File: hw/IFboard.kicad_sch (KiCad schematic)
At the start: 72 parts, among them J1 USB_C_Receptacle_USB2.0_16P, J2 Conn_01x02_Socket, J3 Conn_ARM_SWD_TagConnect_TC203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, J4 Conn_01x02_Socket, J5 Conn_01x02_Socket, J6 Conn_01x02_Socket, SW3 SW_Push, SW4 SW_Push, SW5 SW_Push, SW6 SW_Push, U1 AMS1117-3.3, U2 XC6206PxxxMR, U3 TCAN3413DR, U4 ST4E1240DT, U5 MAX232ESE+T, U6 STM32G0B1CBTx

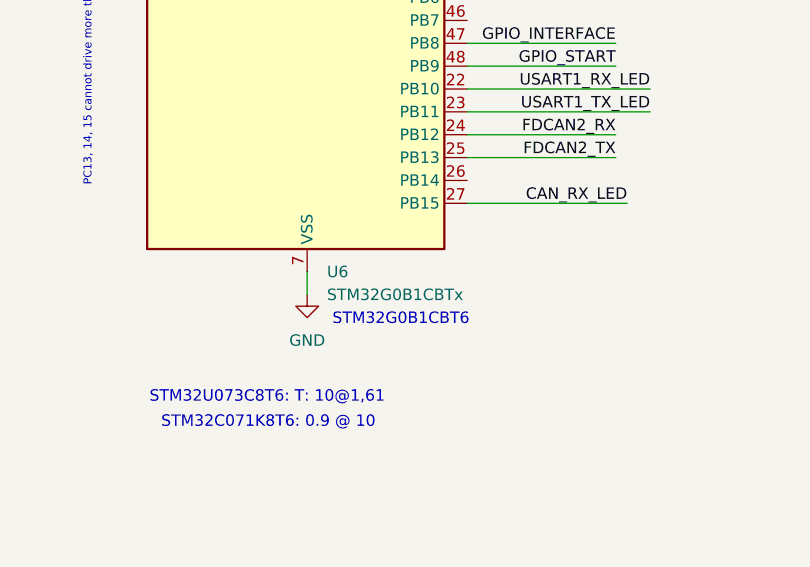
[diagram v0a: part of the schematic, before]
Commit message: copied all parts into personal lib to have JLC numbers added per default
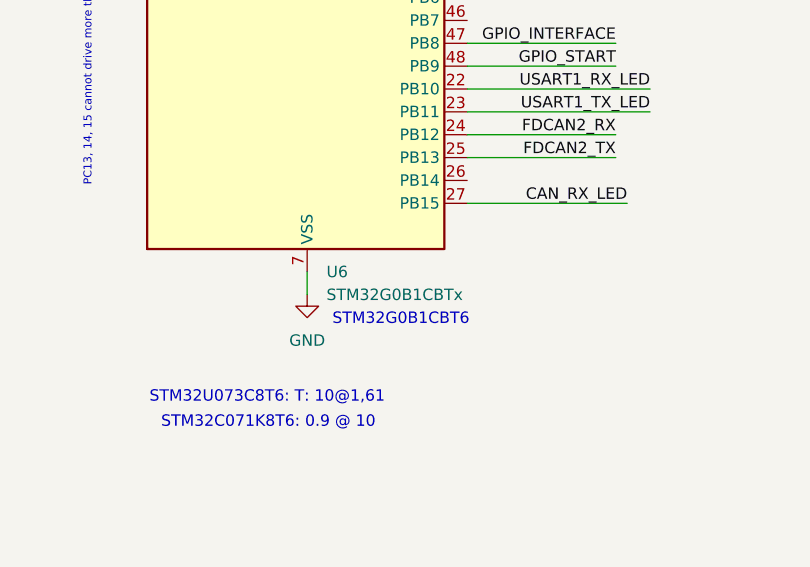
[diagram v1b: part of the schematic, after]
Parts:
- U3: symbol Interface_CAN_LIN:TCAN330 -> PZ:TCAN3413DR
- U4: symbol new:ST4E1240DT -> PZ:ST4E1240DT
- U5: symbol Interface_UART:MAX232 -> PZ:MAX232ESE+T
- U6: symbol MCU_ST_STM32G0:STM32G0B1CBTx -> PZ:STM32G0B1CBTx
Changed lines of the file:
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@@
 	)
 	(symbol
-		(lib_id "new:ST4E1240DT")
+		(lib_id "PZ:ST4E1240DT")
 		(at 297.18 128.27 0)
 		(unit 1)
@@
 	)
 	(symbol
-		(lib_id "MCU_ST_STM32G0:STM32G0B1CBTx")
+		(lib_id "PZ:STM32G0B1CBTx")
 		(at 142.24 213.36 0)
 		(unit 1)
@@
 		(fields_autoplaced yes)
 		(property "Reference" "U6"
-			(at 146.9741 259.08 0)
+			(at 146.9233 259.08 0)
 			(show_name no)
 			(do_not_autoplace no)
@@
 		)
 		(property "Value" "STM32G0B1CBTx"
-			(at 146.9741 261.62 0)
+			(at 146.9233 261.62 0)
 			(show_name no)
 			(do_not_autoplace no)
@@
 	)
 	(symbol
-		(lib_id "Interface_CAN_LIN:TCAN330")
+		(lib_id "PZ:TCAN3413DR")
 		(at 295.91 60.96 0)
 		(unit 1)
@@
 	)
 	(symbol
-		(lib_id "Interface_UART:MAX232")
+		(lib_id "PZ:MAX232ESE+T")
 		(at 297.18 208.28 0)
 		(unit 1)

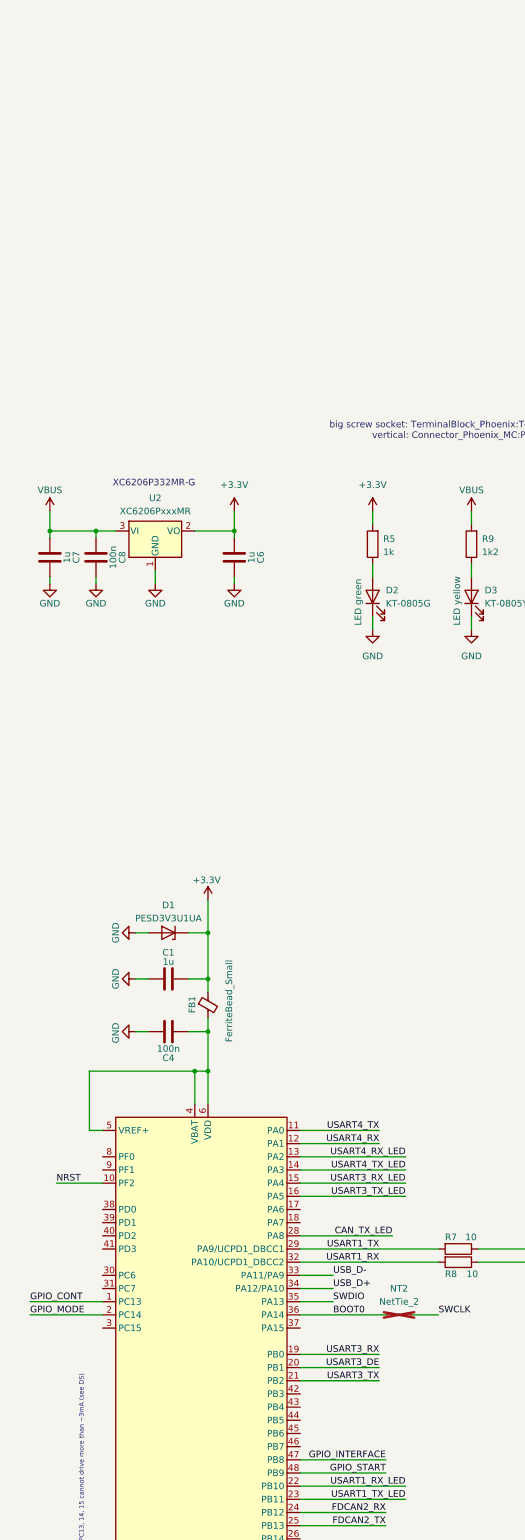
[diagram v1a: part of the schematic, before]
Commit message: wip:add small display
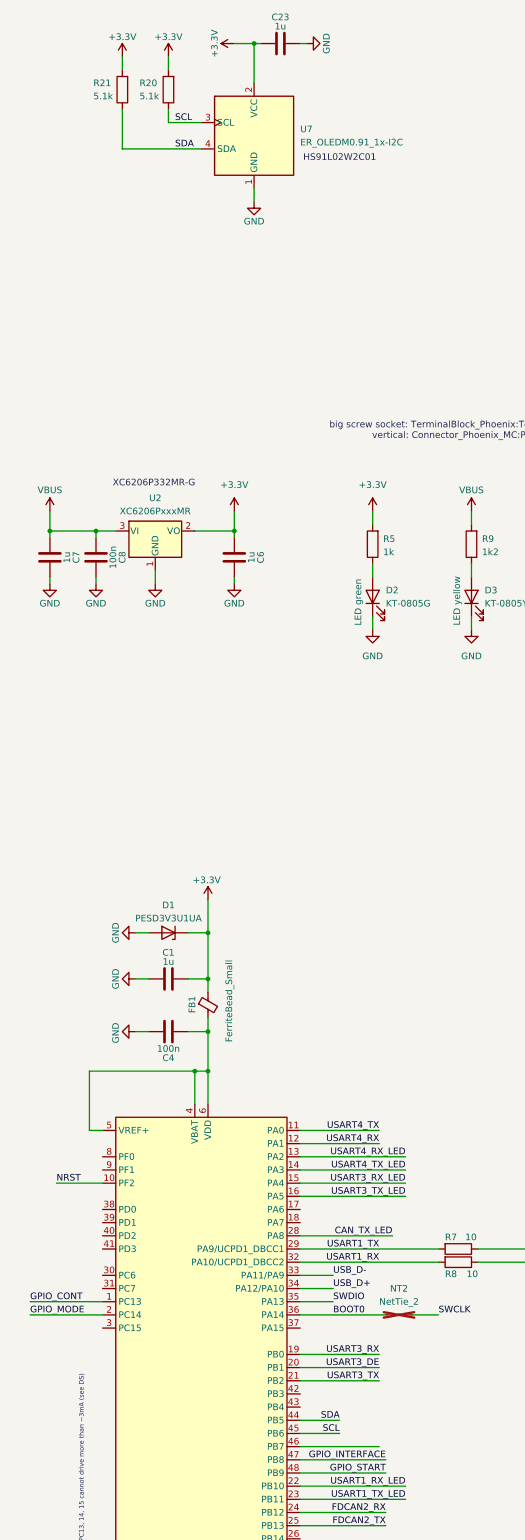
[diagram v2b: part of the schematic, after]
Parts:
- added C23: 1u, Capacitor_SMD:C_0402_1005Metric, symbol Device:C
- added R20, R21: 5.1k, Resistor_SMD:R_0402_1005Metric, symbol Device:R
- added U7: ER_OLEDM0.91_1x-I2C, Display:ER_OLEDM0.91_1x-I2C, symbol Display_Graphic:ER_OLEDM0.91_1x-I2C
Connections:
- net +3.3V: now also C23.2, R20.2, R21.2, U7.2 (VCC)
- net GND: now also C23.1, U7.1 (GND)
- net SDA: now reaches U6.44 (PB5)
- net SDA: now also R21.1, U7.4 (SDA)
- net SCL: now reaches U6.45 (PB6)
- net SCL: now also R20.1, U7.3 (SCL)
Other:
- note added: "HS91L02W2C01"

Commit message: display I2C connection done. not proud of it =)
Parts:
- added R22, R23: 0, Resistor_SMD:R_0603_1608Metric, symbol Device:R
- R7, R8: value 10 -> 0; footprint Resistor_SMD:R_0805_2012Metric -> Resistor_SMD:R_0603_1608Metric; LCSC Part # C17415 -> C21189
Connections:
- net SCL: now also R23.1; no longer U6.45 (PB6)
- net SDA: now also R22.1; no longer U6.44 (PB5)
- new net: R22.2, U6.44 (PB5)
- new net: R23.2, U6.45 (PB6)
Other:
- note added: "just to easy layout without braking the GND plane"
- note removed: "H5VU13U"
- moved on the sheet: C18, C2, C23, C5, C6, C7, C8, D2, D3, D57, R20, R21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

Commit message: forgot last time
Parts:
- removed J6: Conn_01x02_Socket, Connector_Phoenix_MC:PhoenixContact_MC_1,5_2-G-3.5_1x02_P3.50mm_Horizontal, symbol Connector:Conn_01x02_Socket
- added J6: Conn_01x03_Socket, Connector_Phoenix_MC:PhoenixContact_MC_1,5_3-G-3.5_1x03_P3.50mm_Horizontal, symbol Connector:Conn_01x03_Socket
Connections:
- net GND: now also J6.1 (Pin_1)
- net at R15.2, U3.6 (CANL): now also J6.2 (Pin_2)
- net at R14.1, U3.7 (CANH): now also J6.3 (Pin_3)
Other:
- note added: "https://www.icotek.com/en/products/emc-cable-shield-clamps/pcb"
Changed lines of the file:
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@@
 		)
 	)
+	(text "https://www.icotek.com/en/products/emc-cable-shield-clamps/pcb"
+		(exclude_from_sim no)
+		(at 364.744 5.08 0)
+		(effects
+			(font
+				(size 1.27 1.27)
+			)
+		)
+	)
 	(text "just to easy layout without braking the GND plane"
 		(exclude_from_sim no)
@@
 	)
 	(junction
-		(at 327.66 59.69)
+		(at 327.66 73.66)
 		(diameter 0)
 		(color 0 0 0 0)
 	)
 	(junction
-		(at 327.66 46.99)
+		(at 327.66 59.69)
 		(diameter 0)
 		(color 0 0 0 0)
@@
 	)
 	(junction
-		(at 327.66 73.66)
-		(diameter 0)
-		(color 0 0 0 0)
-	)
-	(junction
 		(at 297.18 175.26)
 		(diameter 0)
@@
 	)
 	(junction
+		(at 327.66 46.99)
+		(diameter 0)
+		(color 0 0 0 0)
+	)
+	(junction
 		(at 40.64 205.74)
 		(diameter 0)
@@
 	(wire
 		(pts
-			(xy 356.87 60.96) (xy 356.87 73.66)
+			(xy 351.79 60.96) (xy 351.79 73.66)
 		)
 		(stroke
@@
 	(wire
 		(pts
-			(xy 359.41 58.42) (xy 356.87 58.42)
+			(xy 359.41 58.42) (xy 351.79 58.42)
 		)
 		(stroke
@@
 	(wire
 		(pts
+			(xy 359.41 63.5) (xy 358.14 63.5)
+		)
+		(stroke
+			(width 0)
+			(type default)
+		)
+	)
+	(wire
+		(pts
+			(xy 358.14 63.5) (xy 358.14 67.31)
+		)
+		(stroke
+			(width 0)
+			(type default)
+		)
+	)
+	(wire
+		(pts
 			(xy 316.23 125.73) (xy 316.23 134.62)
 		)
@@
 	(wire
 		(pts
-			(xy 356.87 60.96) (xy 359.41 60.96)
+			(xy 351.79 60.96) (xy 359.41 60.96)
 		)
 		(stroke
@@
 	(wire
 		(pts
-			(xy 356.87 46.99) (xy 356.87 58.42)
+			(xy 351.79 46.99) (xy 351.79 58.42)
 		)
 		(stroke
@@
 	(wire
 		(pts
-			(xy 327.66 46.99) (xy 356.87 46.99)
+			(xy 327.66 46.99) (xy 351.79 46.99)
 		)
 		(stroke
@@
 	(wire
 		(pts
-			(xy 327.66 73.66) (xy 356.87 73.66)
+			(xy 327.66 73.66) (xy 351.79 73.66)
 		)
 		(stroke
@@
 	)
 	(symbol
-		(lib_id "Connector:Conn_01x02_Socket")
-		(at 364.49 60.96 0)
-		(mirror x)
-		(unit 1)
-		(body_style 1)
-		(exclude_from_sim no)
-		(in_bom yes)
-		(on_board yes)
-		(in_pos_files yes)
-		(dnp no)
-		(property "Reference" "J6"
-			(at 364.49 63.754 0)
-			(show_name no)
-			(do_not_autoplace no)
-			(effects
-				(font
-					(size 1.27 1.27)
-				)
-			)
-		)
-		(property "Value" "Conn_01x02_Socket"
-			(at 363.855 63.5 0)
-			(hide yes)
-			(show_name no)
-			(do_not_autoplace no)
-			(effects
-				(font
-					(size 1.27 1.27)
-				)
-			)
-		)
-		(property "Footprint" "Connector_Phoenix_MC:PhoenixContact_MC_1,5_2-G-3.5_1x02_P3.50mm_Horizontal"
-			(at 364.49 60.96 0)
-			(hide yes)
-			(show_name no)
-			(do_not_autoplace no)
-			(effects
-				(font
-					(size 1.27 1.27)
-				)
-			)
-		)
-		(property "Datasheet" ""
-			(at 364.49 60.96 0)
-			(hide yes)
-			(show_name no)
-			(do_not_autoplace no)
-			(effects
-				(font
-					(size 1.27 1.27)
-				)
-			)
-		)
-		(property "Description" "Generic connector, single row, 01x02, script generated"
-			(at 364.49 60.96 0)
-			(hide yes)
-			(show_name no)
-			(do_not_autoplace no)
-			(effects
-				(font
-					(size 1.27 1.27)
-				)
-			)
-		)
-		(property "LCSC Part #" ""
-			(at 364.49 60.96 0)
-			(hide yes)
-			(show_name no)
-			(do_not_autoplace no)
-			(effects
-				(font
-					(size 1.27 1.27)
-				)
-			)
-		)
-		(pin "2"
-		)
-		(pin "1"
-		)
-		(instances
-			(project "IFboard"
-				(path "/5819cdb4-45b5-43a2-a4e4-9ec02e71e355"
-					(reference "J6")
-					(unit 1)
-				)
-			)
-		)
-	)
-	(symbol
 		(lib_id "power:GND")
 		(at 40.64 29.21 270)
@@
 	)
 	(symbol
+		(lib_id "Connector:Conn_01x03_Socket")
+		(at 364.49 60.96 0)
+		(mirror x)
+		(unit 1)
+		(body_style 1)
+		(exclude_from_sim no)
+		(in_bom yes)
+		(on_board yes)
+		(in_pos_files yes)
+		(dnp no)
+		(property "Reference" "J6"
+			(at 363.855 53.34 0)
+			(show_name no)
+			(do_not_autoplace no)
+			(effects
+				(font
+					(size 1.27 1.27)
+				)
+			)
+		)
+		(property "Value" "Conn_01x03_Socket"
+			(at 368.3 51.816 0)
+			(hide yes)
+			(show_name no)
+			(do_not_autoplace no)
+			(effects
+				(font
+					(size 1.27 1.27)
+				)
+			)
+		)
+		(property "Footprint" "Connector_Phoenix_MC:PhoenixContact_MC_1,5_3-G-3.5_1x03_P3.50mm_Horizontal"
+			(at 364.49 60.96 0)
+			(hide yes)
+			(show_name no)
+			(do_not_autoplace no)
+			(effects
+				(font
+					(size 1.27 1.27)
+				)
+			)
+		)
+		(property "Datasheet" ""
+			(at 364.49 60.96 0)
+			(hide yes)
+			(show_name no)
+			(do_not_autoplace no)
+			(effects
+				(font
+					(size 1.27 1.27)
+				)
+			)
+		)
+		(property "Description" "Generic connector, single row, 01x03, script generated"
+			(at 364.49 60.96 0)
+			(hide yes)
+			(show_name no)
+			(do_not_autoplace no)
+			(effects
+				(font
+					(size 1.27 1.27)
+				)
+			)
+		)
+		(property "LCSC Part #" ""
+			(at 364.49 60.96 0)
+			(hide yes)
+			(show_name no)
+			(do_not_autoplace no)
+			(effects
+				(font
+					(size 1.27 1.27)
+				)
+			)
+		)
+		(pin "3"
+		)
+		(pin "2"
+		)
+		(pin "1"
+		)
+		(instances
+			(project "IFboard"
+				(path "/5819cdb4-45b5-43a2-a4e4-9ec02e71e355"
+					(reference "J6")
+					(unit 1)
+				)
+			)
+		)
+	)
+	(symbol
 		(lib_id "Device:C")
 		(at 39.37 270.51 180)
@@
 					(unit 1)
 				)
+			)
+		)
+	)
+	(symbol
+		(lib_id "power:GND")
+		(at 358.14 67.31 0)
+		(unit 1)
+		(body_style 1)
+		(exclude_from_sim no)
+		(in_bom yes)
+		(on_board yes)
+		(in_pos_files yes)
+		(dnp no)
+		(property "Reference" "#PWR068"
+			(at 358.14 73.66 0)
+			(hide yes)
+			(show_name no)
+			(do_not_autoplace no)
+			(effects
+				(font
+					(size 1.27 1.27)
+				)
+			)
+		)
+		(property "Value" "GND"
+			(at 358.394 71.12 0)
+			(show_name no)
+			(do_not_autoplace no)
+			(effects
+				(font
+					(size 1.27 1.27)
+				)
+			)
+		)
+		(property "Footprint" ""
+			(at 358.14 67.31 0)
+			(hide yes)
+			(show_name no)
+			(do_not_autoplace no)
+			(effects
+				(font
+					(size 1.27 1.27)
+				)
+			)
+		)
+		(property "Datasheet" ""
+			(at 358.14 67.31 0)
+			(hide yes)
+			(show_name no)
+			(do_not_autoplace no)
+			(effects
+				(font
+					(size 1.27 1.27)
+				)
+			)
+		)
+		(property "Description" "Power symbol creates a global label with name \"GND\" , ground"
+			(at 358.14 67.31 0)
+			(hide yes)
+			(show_name no)
+			(do_not_autoplace no)
+			(effects
+				(font
+					(size 1.27 1.27)
+				)
+			)
+		)
+		(pin "1"
+		)
+		(instances
+			(project "IFboard"
+				(path "/5819cdb4-45b5-43a2-a4e4-9ec02e71e355"
+					(reference "#PWR068")
+					(unit 1)
+				)

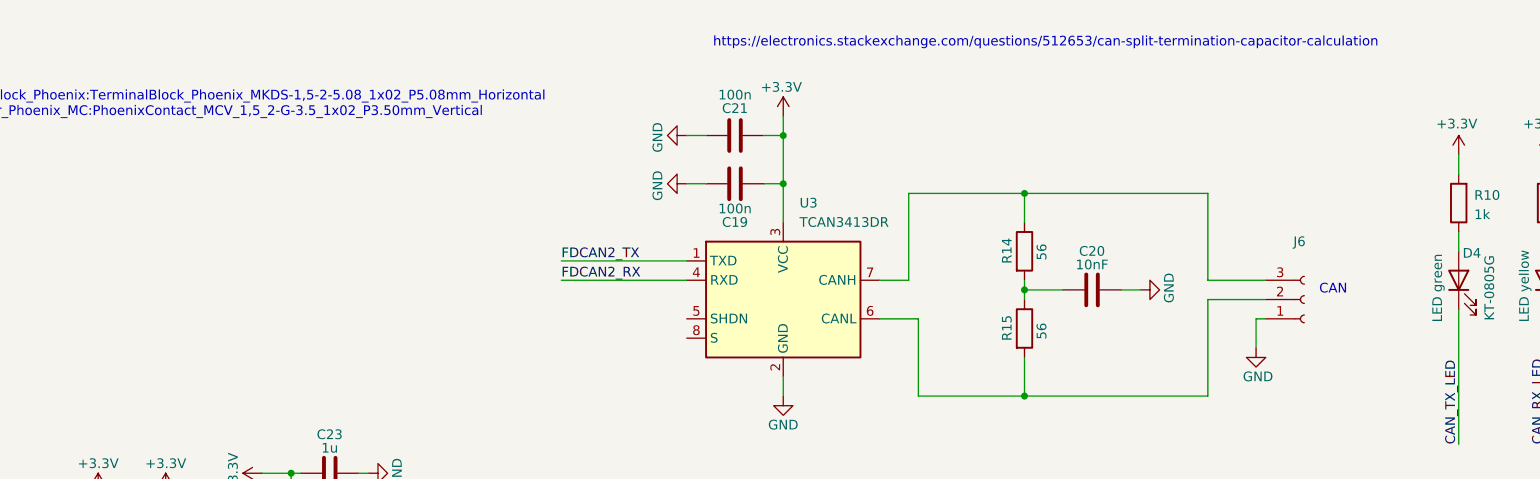
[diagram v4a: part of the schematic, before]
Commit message: tag:3.5mm connectors
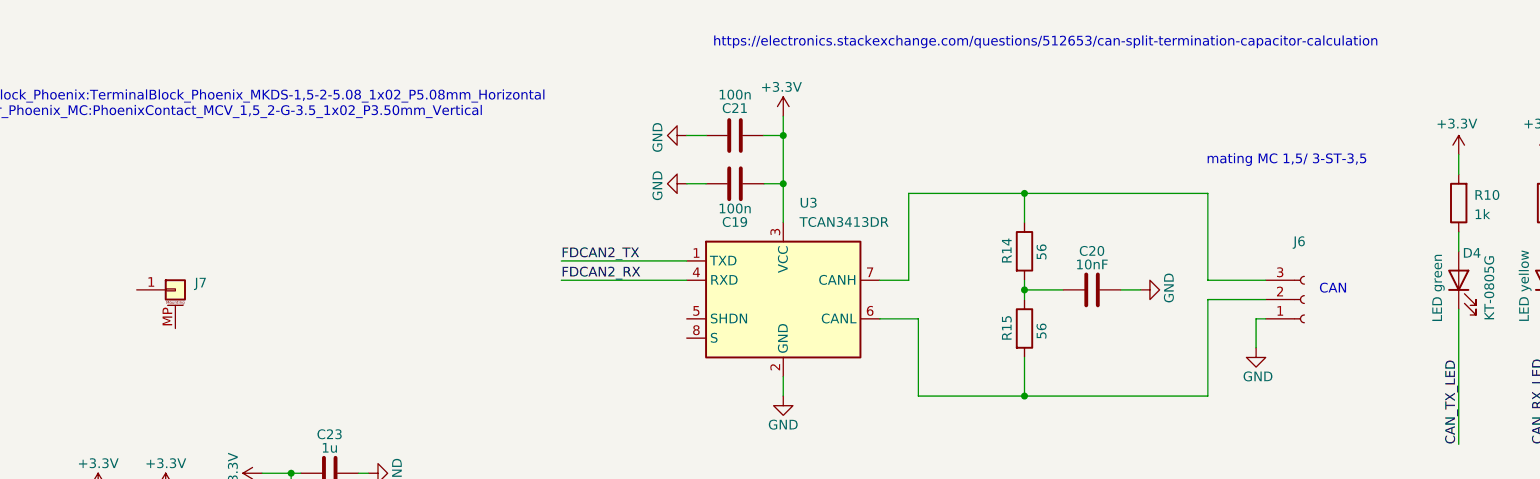
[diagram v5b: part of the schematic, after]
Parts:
- added J7: Conn_01x01_MountingPin, Connector_PinHeader_1.00mm:PinHeader_1x01_P1.00mm_Vertical, symbol Connector_Generic_MountingPin:Conn_01x01_MountingPin
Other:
- note added: "mating MC 1,5/ 3-ST-3,5"
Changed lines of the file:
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@@
 		)
 	)
+	(text "mating MC 1,5/ 3-ST-3,5"
+		(exclude_from_sim no)
+		(at 362.204 42.672 0)
+		(effects
+			(font
+				(size 1.27 1.27)
+			)
+		)
+	)
 	(text "https://electronics.stackexchange.com/questions/512653/can-split-termination-capacitor-calculation"
 		(exclude_from_sim no)
@@
 					(unit 1)
 				)
+			)
+		)
+	)
+	(symbol
+		(lib_id "Connector_Generic_MountingPin:Conn_01x01_MountingPin")
+		(at 215.9 59.69 0)
+		(unit 1)
+		(body_style 1)
+		(exclude_from_sim no)
+		(in_bom yes)
+		(on_board yes)
+		(in_pos_files yes)
+		(dnp no)
+		(fields_autoplaced yes)
+		(property "Reference" "J7"
+			(at 218.44 58.7755 0)
+			(show_name no)
+			(do_not_autoplace no)
+			(effects
+				(font
+					(size 1.27 1.27)
+				)
+				(justify left)
+			)
+		)
+		(property "Value" "Conn_01x01_MountingPin"
+			(at 218.44 61.3155 0)
+			(hide yes)
+			(show_name no)
+			(do_not_autoplace no)
+			(effects
+				(font
+					(size 1.27 1.27)
+				)
+				(justify left)
+			)
+		)
+		(property "Footprint" "Connector_PinHeader_1.00mm:PinHeader_1x01_P1.00mm_Vertical"
+			(at 215.9 59.69 0)
+			(hide yes)
+			(show_name no)
+			(do_not_autoplace no)
+			(effects
+				(font
+					(size 1.27 1.27)
+				)
+			)
+		)
+		(property "Datasheet" ""
+			(at 215.9 59.69 0)
+			(hide yes)
+			(show_name no)
+			(do_not_autoplace no)
+			(effects
+				(font
+					(size 1.27 1.27)
+				)
+			)
+		)
+		(property "Description" "Generic connectable mounting pin connector, single row, 01x01, script generated (kicad-library-utils/schlib/autogen/connector/)"
+			(at 215.9 59.69 0)
+			(hide yes)
+			(show_name no)
+			(do_not_autoplace no)
+			(effects
+				(font
+					(size 1.27 1.27)
+				)
+			)
+		)
+		(property "LCSC Part #" ""
+			(at 215.9 59.69 0)
+			(hide yes)
+			(show_name no)
+			(do_not_autoplace no)
+			(effects
+				(font
+					(size 1.27 1.27)
+				)
+			)
+		)
+		(pin "MP"
+		)
+		(pin "1"
+		)
+		(instances
+			(project "IFboard"
+				(path "/5819cdb4-45b5-43a2-a4e4-9ec02e71e355"
+					(reference "J7")
+					(unit 1)
+				)

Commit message: wip
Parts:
- removed J2, J4, J5: Conn_01x02_Socket, Connector_Phoenix_MC:PhoenixContact_MC_1,5_2-G-3.5_1x02_P3.50mm_Horizontal, symbol Connector:Conn_01x02_Socket
- added J2, J4, J5: Conn_01x03_Socket, PZL:1881451, symbol Connector:Conn_01x03_Socket
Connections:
- net GND: now also J6.3 (Pin_3), J2.3 (Pin_3), J4.3 (Pin_3), J5.3 (Pin_3); no longer J6.1 (Pin_1)
- net USART4_RX_MAX: now also J5.2 (Pin_2)
- net USART4_TX_MAX: now also J5.1 (Pin_1)
- net at R7.1: now also J2.1 (Pin_1)
- net at R8.1: now also J2.2 (Pin_2)
- net at JP1.1 (A), U4.6 (A): now also J4.1 (Pin_1)
- net at R6.1, U4.7 (B): now also J4.2 (Pin_2)
- net at R15.2, U3.6 (CANL): now also J6.1 (Pin_1); no longer J6.2 (Pin_2)
- net at R14.1, U3.7 (CANH): now also J6.2 (Pin_2); no longer J6.3 (Pin_3)
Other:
- note added: "FK-MC 0,5/ 3-ST-2,5"
- note added: "MC_1,5_3-G-3.5_1x03_P3.50mm"
- note added: "mating (for 0,2-1,5 mm2) MC 1,5/3-ST-3,5 FMC 1,5/3-ST-3,5"
- note removed: "mating MC 1,5/ 3-ST-3,5"
